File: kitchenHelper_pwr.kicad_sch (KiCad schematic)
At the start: 12 parts, among them IC2 FS312F-G, IC3 VReg 3v3, J6 Charger, J7 Battery, Q6 FS8205

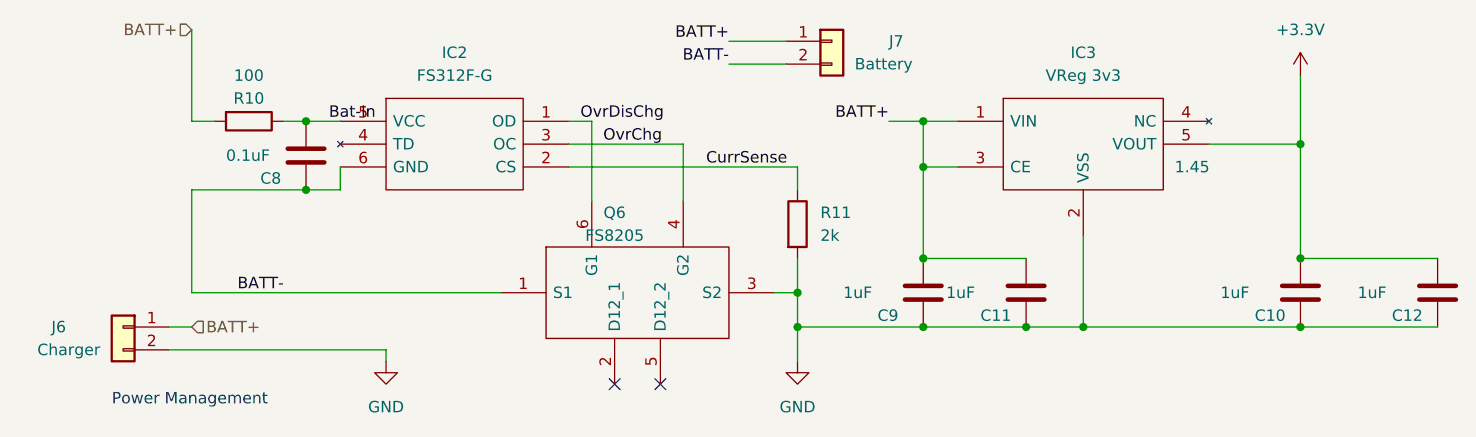
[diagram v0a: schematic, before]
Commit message: Migrated project to KiCad7
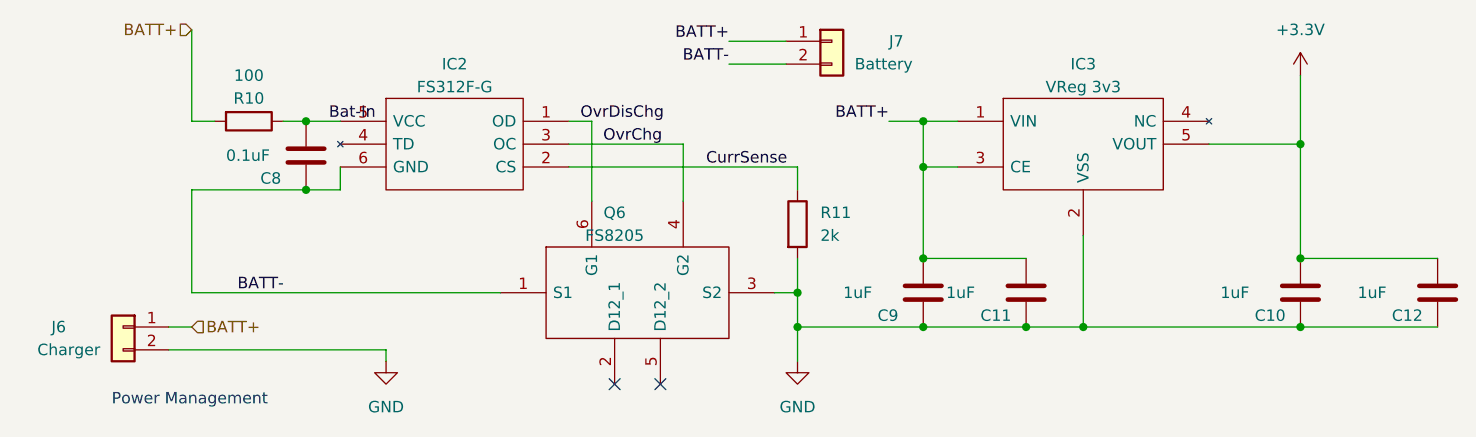
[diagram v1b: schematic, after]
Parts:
- IC2: footprint footprints:SOT95P280X145-6N -> SOT95P280X145-6N; symbol Li-Ion Charging:FS312F-G -> Chof747 Battery Management:FS312F-G
- IC3: footprint footprints:SOT95P270X145-5N -> SOT95P270X145-5N; symbol Regulator_Linear:ME6211C33M5G-N -> Chof747 Voltage Regulators:ME6211C33M5G-N
- Q6: footprint footprints:FS8205 -> FS8205; symbol FS8205:FS8205 -> Chof747 Transistors and Mosfets:FS8205
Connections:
- net +3V3 renamed +3.3V
